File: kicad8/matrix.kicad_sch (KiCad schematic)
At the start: 171 parts

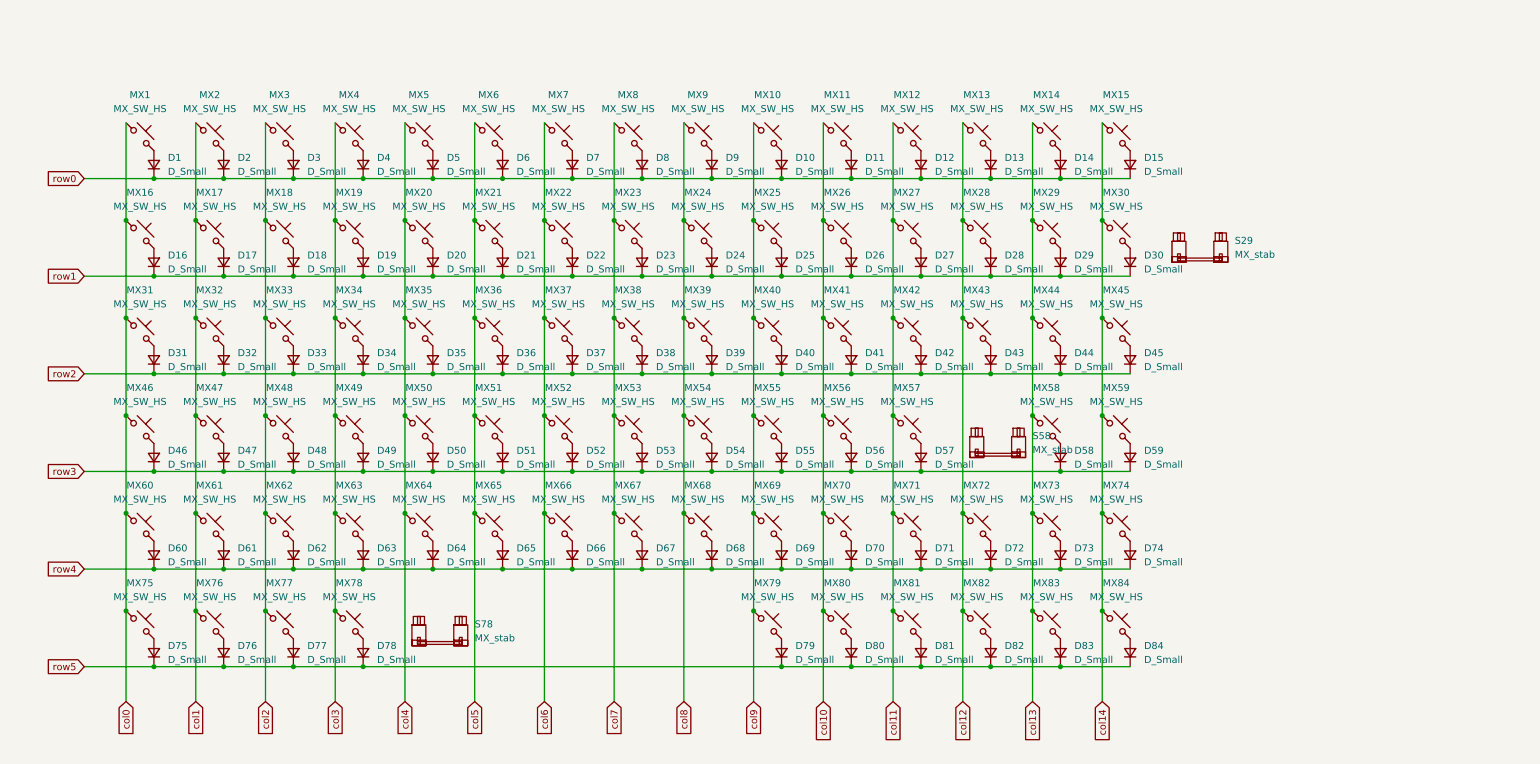
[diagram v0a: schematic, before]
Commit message: Changed: switch footprint
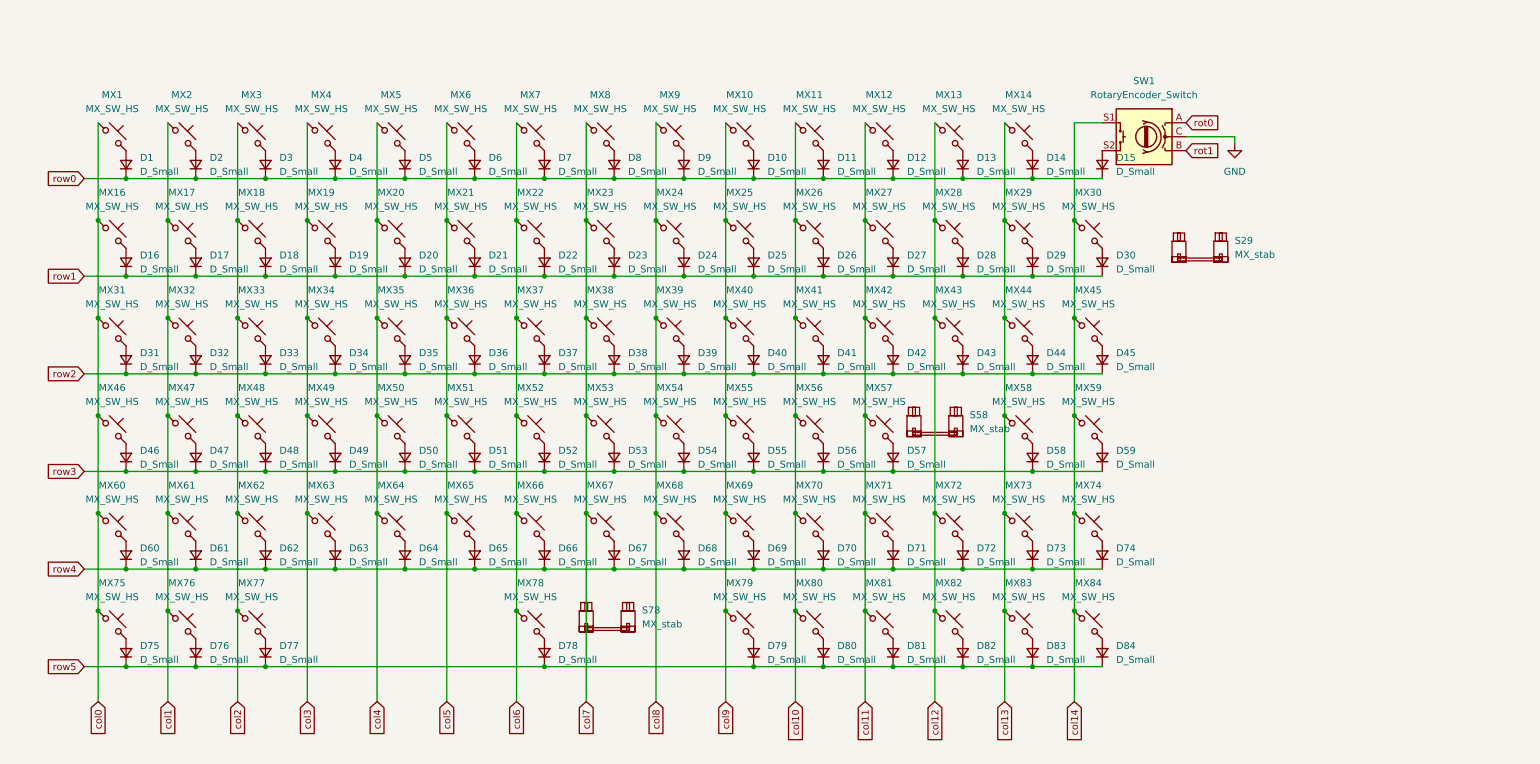
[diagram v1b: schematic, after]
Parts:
- removed MX15: MX_SW_HS, MX_Hotswap:MX-Hotswap-1U, symbol PCM_marbastlib-mx:MX_SW_HS_CPG151101S11
- removed S58: MX_stab, PCM_marbastlib-mx:STAB_MX_P_2.25u, symbol PCM_marbastlib-mx:MX_stab
- added S78: MX_stab, PCM_marbastlib-mx:STAB_MX_P_6.25u, symbol PCM_marbastlib-mx:MX_stab
- added SW1: RotaryEncoder_Switch, Rotary_Encoder:RotaryEncoder_Alps_EC11E-Switch_Vertical_H20mm, symbol Device:RotaryEncoder_Switch
- MX1, MX10, MX11, MX12, MX13, MX14, MX16, MX17, MX18, MX19, MX2, MX20, MX21, MX22, MX23, MX24, MX25, MX26, MX27, MX28, MX29, MX3, MX30, MX31, MX32, MX33, MX34, MX35, MX36, MX37, MX38, MX39, MX4, MX40, MX41, MX42, MX43, MX44, MX45, MX46, MX47, MX48, MX49, MX5, MX50, MX51, MX52, MX53, MX54, MX55, MX56, MX57, MX58, MX59, MX6, MX60, MX61, MX62, MX63, MX64, MX65, MX66, MX67, MX68, MX69, MX7, MX70, MX71, MX72, MX73, MX74, MX75, MX76, MX77, MX78, MX79, MX8, MX80, MX81, MX82, MX83, MX84, MX9: footprint MX_Hotswap:MX-Hotswap-1U -> PCM_marbastlib-mx:SW_MX_HS_CPG151101S11_1u
- S58: renamed from S78; footprint PCM_marbastlib-mx:STAB_MX_P_6.25u -> PCM_marbastlib-mx:STAB_MX_P_2.25u
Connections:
- net col14: now also SW1.S1
- net col3: no longer MX78.1
- net col6: now also MX78.1
- net at D15.2 (A): now also SW1.S2
- new net GND: SW1.C
- new net rot0: SW1.A
- new net rot1: SW1.B
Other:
- moved on the sheet: S58

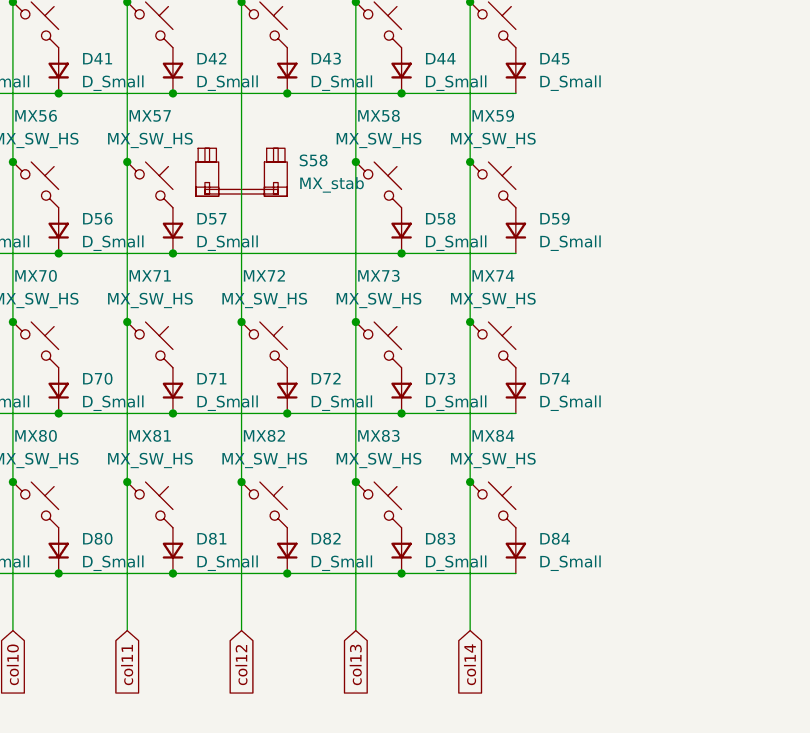
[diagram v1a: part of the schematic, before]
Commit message: Changed: Switch matrix layout
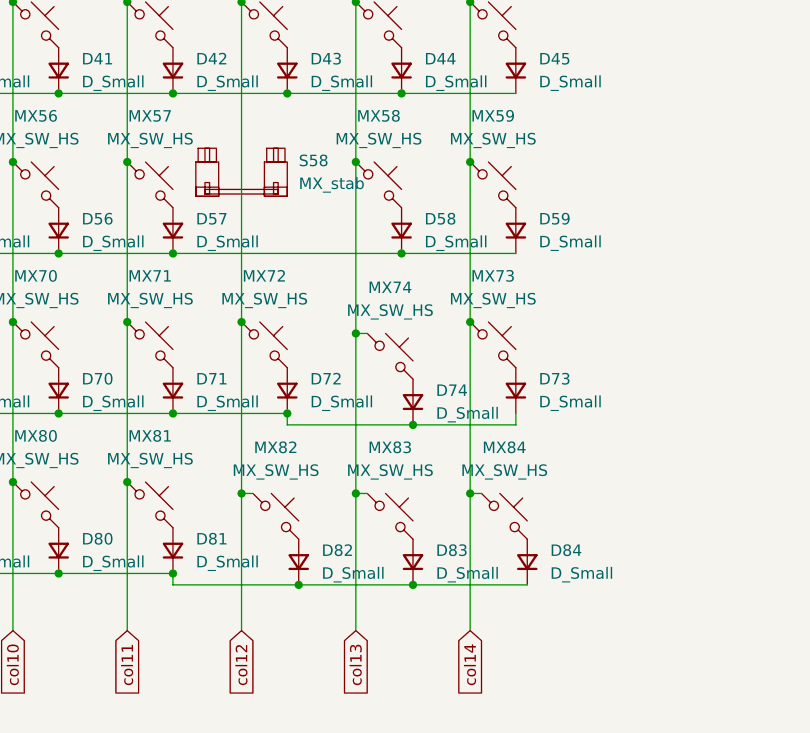
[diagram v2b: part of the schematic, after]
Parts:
- removed D73: D_Small, Diode_SMD:D_SOD-123, symbol Device:D_Small
- added D74: D_Small, Diode_SMD:D_SOD-123, symbol Device:D_Small
- SW1: footprint Rotary_Encoder:RotaryEncoder_Alps_EC11E-Switch_Vertical_H20mm -> PCM_marbastlib-various:ROT_Alps_EC11E-Switch
- renumbered D74 to D73, MX74 to MX73, MX73 to MX74
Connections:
- net row4: now also D74.1 (K)
- net at MX74.2: now also D74.2 (A)
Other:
- moved on the sheet: D82, D83, D84, MX74, MX82, MX83, MX84

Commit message: Added: Stepped CAPS_LOCK and Split backspace
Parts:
- removed MX76, MX77: MX_SW_HS, PCM_marbastlib-mx:SW_MX_HS_CPG151101S11_1u, symbol PCM_marbastlib-mx:MX_SW_HS_CPG151101S11
- removed S29: MX_stab, PCM_marbastlib-mx:STAB_MX_P_2u, symbol PCM_marbastlib-mx:MX_stab
- removed SW1: RotaryEncoder_Switch, PCM_marbastlib-various:ROT_Alps_EC11E-Switch, symbol Device:RotaryEncoder_Switch
- added D29: D_Small, Diode_SMD:D_SOD-123, symbol Device:D_Small
- added MX28, MX30: MX_SW_solder, PCM_marbastlib-mx:SW_MX_1u, symbol PCM_marbastlib-mx:MX_SW_solder
- added MX48: MX_SW_HS, PCM_marbastlib-mx:SW_MX_HS_S_CPG151101S11_1u, symbol PCM_marbastlib-mx:MX_SW_HS_CPG151101S11
- added MX78, MX79: MX_SW_HS, PCM_marbastlib-mx:SW_MX_HS_CPG151101S11_1.25u, symbol PCM_marbastlib-mx:MX_SW_HS_CPG151101S11
- added MX87: MX_SW_HS, PCM_marbastlib-mx:SW_MX_HS_CPG151101S11_1u, symbol PCM_marbastlib-mx:MX_SW_HS_CPG151101S11
- added Q2: Q_PMOS_GSD, symbol Device:Q_PMOS_GSD
- added R6: 10k, Diode_SMD:D_SOD-123, symbol Device:R_Small
- added SW1: ROT_SKYLOONG_HS, PCM_marbastlib-various:ROT_SKYLOONG_HS-Switch, symbol PCM_marbastlib-various:ROT_SKYLOONG_HS-Switch
- MX32: renamed from MX31; footprint PCM_marbastlib-mx:SW_MX_HS_CPG151101S11_1u -> PCM_marbastlib-mx:SW_MX_HS_CPG151101S11_1.5u
- MX45: renamed from MX44; footprint PCM_marbastlib-mx:SW_MX_HS_CPG151101S11_1u -> PCM_marbastlib-mx:SW_MX_HS_CPG151101S11_1.5u
- MX74: renamed from MX72; footprint PCM_marbastlib-mx:SW_MX_HS_CPG151101S11_1u -> PCM_marbastlib-mx:SW_MX_HS_CPG151101S11_1.75u
- MX77: renamed from MX75; footprint PCM_marbastlib-mx:SW_MX_HS_CPG151101S11_1u -> PCM_marbastlib-mx:SW_MX_HS_CPG151101S11_1.25u
- renumbered D29 to D30, D30 to D31, D31 to D32, D32 to D33, D33 to D34, D34 to D35, D35 to D36, D36 to D37, D37 to D38, D38 to D39, D39 to D40, D40 to D41, D41 to D42, D42 to D43, D43 to D44, D44 to D45, D45 to D46, D46 to D47, D47 to D48, D48 to D49, D49 to D50, D50 to D51, D51 to D52, D52 to D53, D53 to D54, D54 to D55, D55 to D56, D56 to D57, D57 to D58, D58 to D59, D59 to D60, D60 to D61, D61 to D62, D62 to D63, D63 to D64, D64 to D65, D65 to D66, D66 to D67, D67 to D68, D68 to D69, D69 to D70, D70 to D71, D71 to D72, D72 to D73, D73 to D74, D74 to D75, D75 to D76, D76 to D77, D77 to D78, D78 to D79, D79 to D80, D80 to D81, D81 to D82, D82 to D83, D83 to D84, D84 to D85, MX16 to MX15, MX17 to MX16, MX18 to MX17, MX19 to MX18, MX20 to MX19, MX21 to MX20, MX22 to MX21, MX23 to MX22, MX24 to MX23, MX25 to MX24, MX26 to MX25, MX27 to MX26, MX28 to MX27, MX30 to MX31, MX32 to MX33, MX33 to MX34, MX34 to MX35, MX35 to MX36, MX36 to MX37, MX37 to MX38, MX38 to MX39, MX39 to MX40, MX40 to MX41, MX41 to MX42, MX42 to MX43, MX43 to MX44, MX45 to MX46, MX46 to MX47, MX47 to MX49, MX48 to MX50, MX49 to MX51, MX50 to MX52, MX51 to MX53, MX52 to MX54, MX53 to MX55, MX54 to MX56, MX55 to MX57, MX56 to MX58, MX57 to MX59, MX58 to MX60, MX59 to MX61, MX60 to MX62, MX61 to MX63, MX62 to MX64, MX63 to MX65, MX64 to MX66, MX65 to MX67, MX66 to MX68, MX67 to MX69, MX68 to MX70, MX69 to MX71, MX70 to MX72, MX71 to MX73, MX73 to MX75, MX74 to MX76, MX78 to MX80, MX79 to MX81, MX80 to MX82, MX81 to MX83, MX82 to MX84, MX83 to MX85, MX84 to MX86, S58 to S1, S78 to S2
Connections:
- net GND: now also SW1.C
- net col0: now also MX48.1
- net col1: now also MX78.1
- net col12: now also MX28.1
- net col13: now also MX30.1
- net col14: now also MX87.1, Q2.2 (S)
- net col2: now also MX79.1
- net rot0: now also SW1.A
- net rot1: now also SW1.B
- net row3: now also D29.1 (K)
- net at D15.2 (A): now also MX87.2, Q2.3 (D)
- net at D78.2 (A): now also MX79.2
- net at D30.2 (A), MX29.2: now also MX30.2
- net at D77.2 (A): now also MX78.2
- net at D47.2 (A), MX47.2: now also MX48.2
- new net: Q2.1 (G), R6.1, SW1.S
- new net: D29.2 (A), MX28.2
- new net VDD: R6.2
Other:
- moved on the sheet: D30, D31, MX29, MX31, MX47

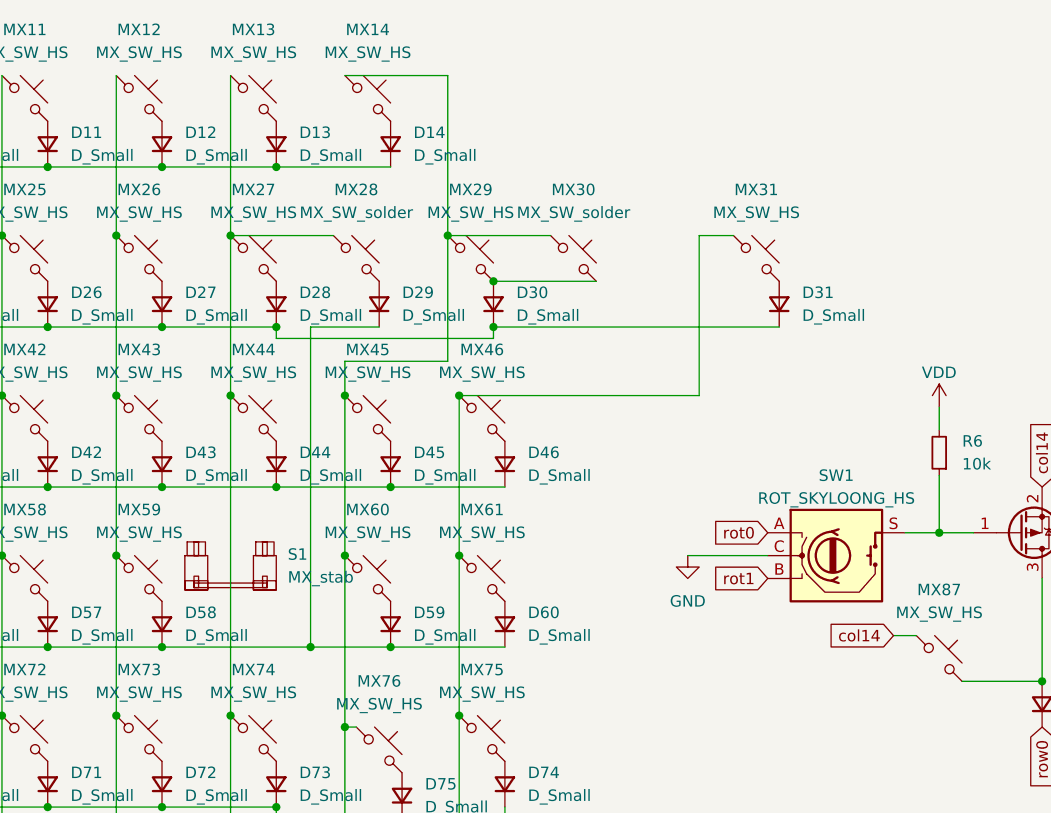
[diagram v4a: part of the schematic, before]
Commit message: Finished: Wiring for the Switch matrix, Underglow RGB and Per-key RGb
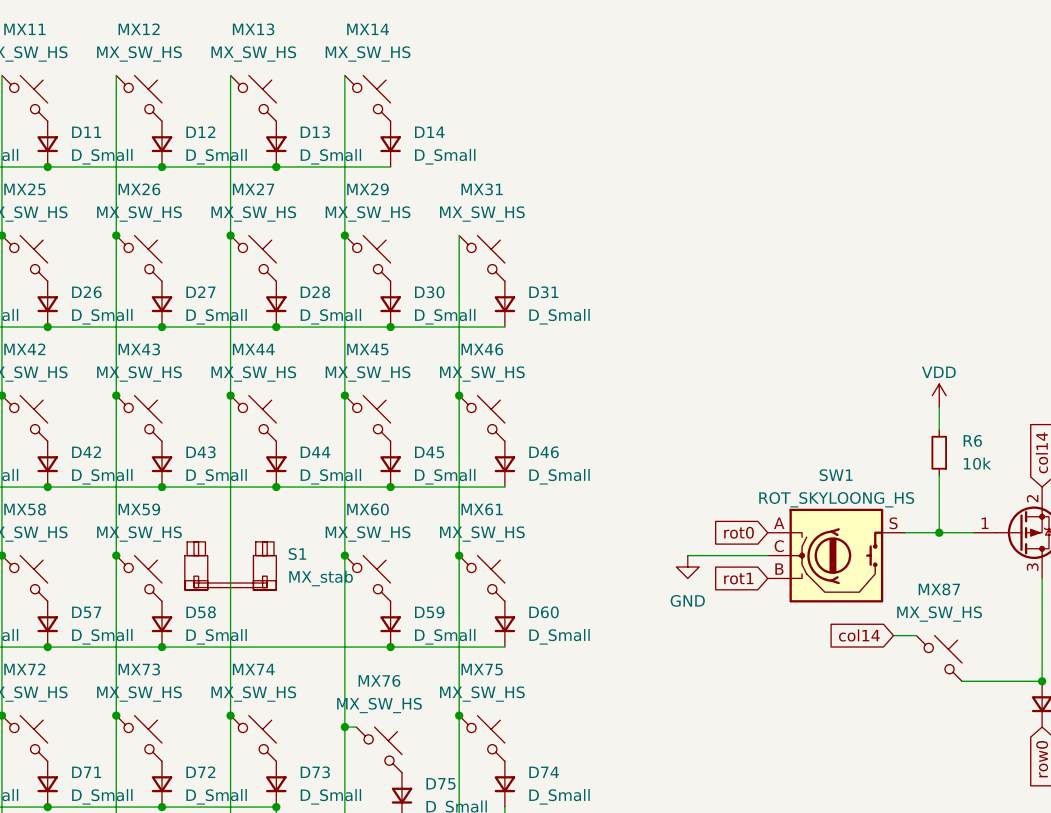
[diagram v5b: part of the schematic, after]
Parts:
- removed D29: D_Small, Diode_SMD:D_SOD-123, symbol Device:D_Small
- removed MX28, MX30: MX_SW_solder, PCM_marbastlib-mx:SW_MX_1u, symbol PCM_marbastlib-mx:MX_SW_solder
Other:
- moved on the sheet: D30, D31, MX29, MX31

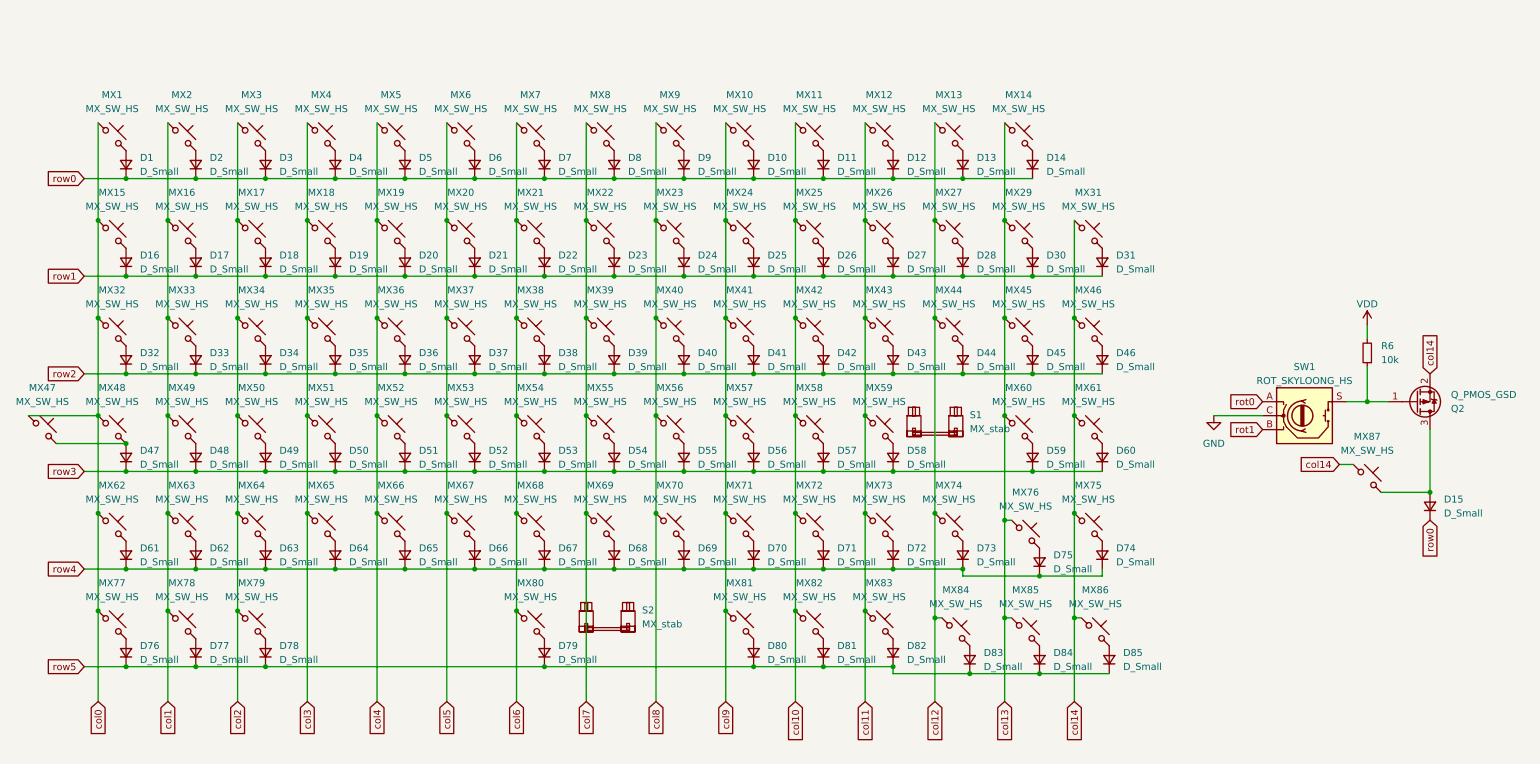
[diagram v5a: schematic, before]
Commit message: Added: MOSFET for encoder and drill holes for case
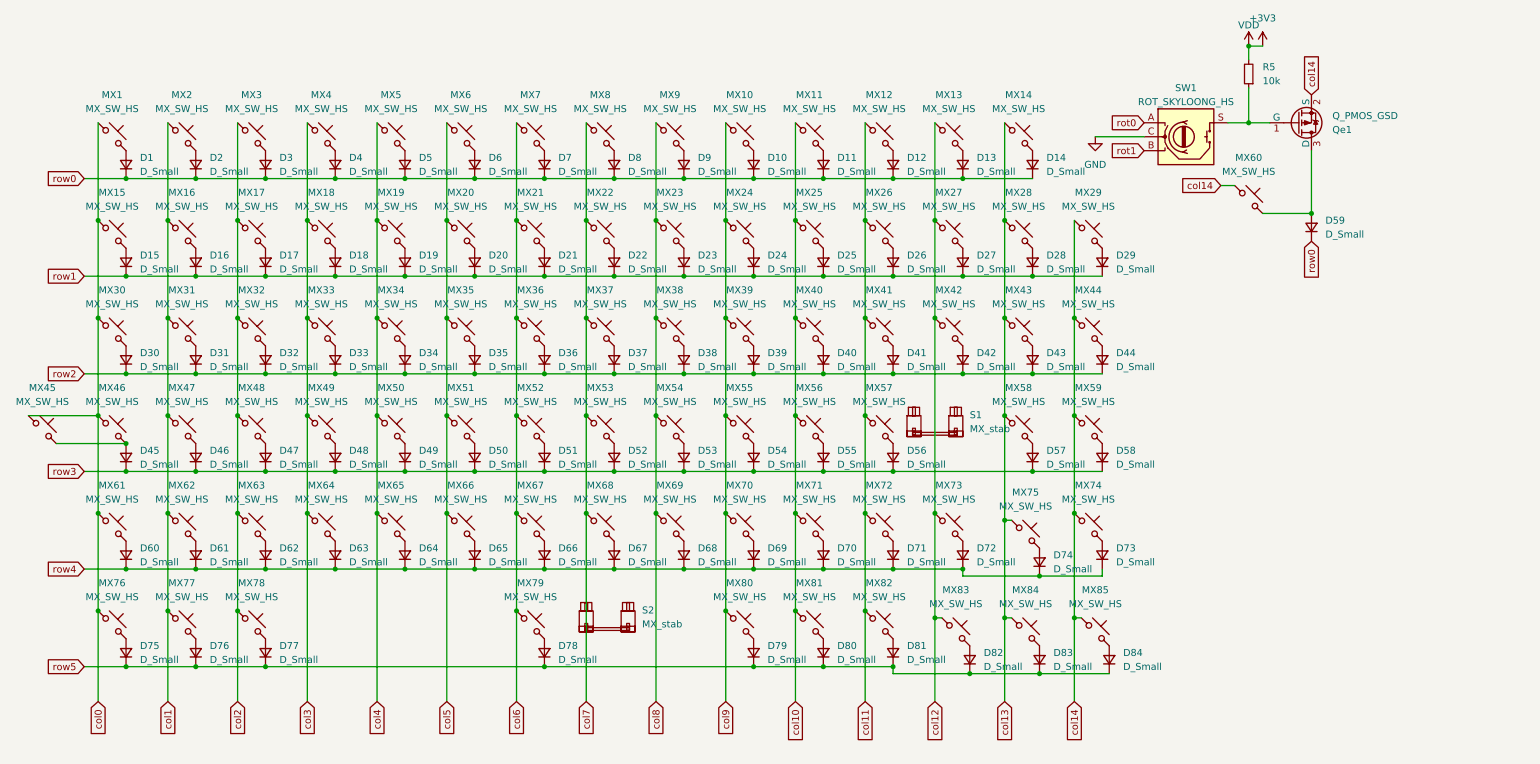
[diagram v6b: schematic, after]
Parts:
- Qe1: renamed from Q2; footprint (none) -> Package_TO_SOT_SMD:SOT-23
- renumbered D16 to D15, D17 to D16, D18 to D17, D19 to D18, D20 to D19, D21 to D20, D22 to D21, D23 to D22, D24 to D23, D25 to D24, D26 to D25, D27 to D26, D28 to D27, D30 to D28, D31 to D29, D32 to D30, D33 to D31, D34 to D32, D35 to D33, D36 to D34, D37 to D35, D38 to D36, D39 to D37, D40 to D38, D41 to D39, D42 to D40, D43 to D41, D44 to D42, D45 to D43, D46 to D44, D47 to D45, D48 to D46, D49 to D47, D50 to D48, D51 to D49, D52 to D50, D53 to D51, D54 to D52, D55 to D53, D56 to D54, D57 to D55, D58 to D56, D59 to D57, D60 to D58, D15 to D59, D61 to D60, D62 to D61, D63 to D62, D64 to D63, D65 to D64, D66 to D65, D67 to D66, D68 to D67, D69 to D68, D70 to D69, D71 to D70, D72 to D71, D73 to D72, D74 to D73, D75 to D74, D76 to D75, D77 to D76, D78 to D77, D79 to D78, D80 to D79, D81 to D80, D82 to D81, D83 to D82, D84 to D83, D85 to D84, MX29 to MX28, MX31 to MX29, MX32 to MX30, MX33 to MX31, MX34 to MX32, MX35 to MX33, MX36 to MX34, MX37 to MX35, MX38 to MX36, MX39 to MX37, MX40 to MX38, MX41 to MX39, MX42 to MX40, MX43 to MX41, MX44 to MX42, MX45 to MX43, MX46 to MX44, MX47 to MX45, MX48 to MX46, MX49 to MX47, MX50 to MX48, MX51 to MX49, MX52 to MX50, MX53 to MX51, MX54 to MX52, MX55 to MX53, MX56 to MX54, MX57 to MX55, MX58 to MX56, MX59 to MX57, MX60 to MX58, MX61 to MX59, MX87 to MX60, MX62 to MX61, MX63 to MX62, MX64 to MX63, MX65 to MX64, MX66 to MX65, MX67 to MX66, MX68 to MX67, MX69 to MX68, MX70 to MX69, MX71 to MX70, MX72 to MX71, MX73 to MX72, MX74 to MX73, MX75 to MX74, MX76 to MX75, MX77 to MX76, MX78 to MX77, MX79 to MX78, MX80 to MX79, MX81 to MX80, MX82 to MX81, MX83 to MX82, MX84 to MX83, MX85 to MX84, MX86 to MX85, R6 to R5
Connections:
- net VDD renamed +3V3
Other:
- moved on the sheet: D59, MX60, R5, SW1
